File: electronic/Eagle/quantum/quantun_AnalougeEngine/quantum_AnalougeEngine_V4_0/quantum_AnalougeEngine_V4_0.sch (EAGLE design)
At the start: 167 parts, among them IC1 OP275, IC10 NE5532D, IC2 NE5532D, IC3 NE5532D, IC4 OP275, IC5 NE5532D, IC6 NE5532D, IC7 NE5532D, IC8 OP275, IC9 TL072, K5 RELAY_EE2-5NU, K6 RELAY_EE2-5NU, K7 RELAY_EE2-5NU, K8 RELAY_EE2-5NU, U1 NUCLEO-F429ZI, U12 ULN2003, U4 THAT1240, U6 THAT1240, U7 THAT1240, U8 THAT1240

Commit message: quantum_AnalougueEngine V4_0
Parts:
- removed C59, C64: 100nF, C_Sager_Bibliothek:CAPACITOR"
- removed C69, C70: 2.2µF, C_Sager_Bibliothek:SMD_ELCTROLYTIC
- removed D1, D2, D3, D4, D5, D6, D7, D8: 4148, C_Sager_Bibliothek:4148
- removed IC10, IC6: NE5532D, linear:NE5532D
- removed TP04: TPTHT, C_Sager_Bibliothek:TPTHT
- added C33, C34, C39, C40, C44: 10 µF, C_Sager_Bibliothek:ELECTROLYTHICELCTROLYTIC_MIDSIZE_SMD
- added C35, C36, C43, C45, C46, C47, C48, C49, C50: 100nF, C_Sager_Bibliothek:CAPACITOR"
- added C37, C38: 22pF, C_Sager_Bibliothek:CAPACITOR"
- added R36, R37: 20k, C_Sager_Bibliothek:RESISTOR
- added R38, R41, R44, R64: 51k, C_Sager_Bibliothek:RESISTOR
- added R39, R42, R45, R65: 51R, C_Sager_Bibliothek:RESISTOR
- added R40, R43, R63, R66: 90k9, C_Sager_Bibliothek:RESISTOR
- added R46, R68, R69, R70, R71, R72, R73, R74, R75: 10k, C_Sager_Bibliothek:RESISTOR
- added R47, R76: 1k8, C_Sager_Bibliothek:RESISTOR
- added R77: 0R, C_Sager_Bibliothek:RESISTOR
- added STAGE(LEFT), STAGE(RIGHT): THAT2181S, THAT_Library:THAT2181S
- added U$4: AD7606_EVALBOARD, C_Sager_Bibliothek:AD7606_EVALBOARD
- added Z1: BZT52C2V0T-7, C_Sager_Bibliothek:BZT52C2V0T-7
- C10, C16, C17, C9: value 100nF -> 470 pF
- C15, C18: value 100nF -> 47 pF
- C31, C32: value 100nF -> 10 µF; device C_Sager_Bibliothek:CAPACITOR" -> C_Sager_Bibliothek:ELECTROLYTHICELCTROLYTIC_MIDSIZE_SMD
- C67, C68: device C_Sager_Bibliothek:SMD_ELCTROLYTIC -> C_Sager_Bibliothek:ELECTROLYTHICELCTROLYTIC_MIDSIZE_SMD
- IC2, IC3: value NE5532D -> DAC084S085CIMM_NOPB; device linear:NE5532D -> SPI:DAC084S085CIMM_NOPB; SPICEPREFIX Z -> (none)
- IC5: value NE5532D -> OP275; device linear:NE5532D -> C_Sager_Bibliothek:OP275; SPICEPREFIX Z -> (none)
- IC7: value NE5532D -> TL072; device linear:NE5532D -> C_Sager_Bibliothek:TL072; SPICEPREFIX Z -> (none)
- K1: value RELAY_EE2-5NU -> K1
- K2: value RELAY_EE2-5NU -> K2
- K3: value RELAY_EE2-5NU -> K3
- K4: value RELAY_EE2-5NU -> K4
- R1, R16, R17, R23, R25, R27, R4, R6: value 100k -> 10k; device C_Sager_Bibliothek:RESISTOR" -> C_Sager_Bibliothek:RESISTOR
- R10, R11, R12, R2, R33, R34, R35, R48, R49, R50, R51, R52, R53, R9: device C_Sager_Bibliothek:RESISTOR" -> C_Sager_Bibliothek:RESISTOR
- R13, R18, R20, R22: value 100k -> 10k; device C_Sager_Bibliothek:RESISTOR" -> C_Sager_Bibliothek:RESISTOR; SPICEPREFIX (none) -> R
- R14, R29: value 0R -> 220R; device C_Sager_Bibliothek:RESISTOR" -> C_Sager_Bibliothek:RESISTOR
- R15, R24: value 0R -> 10k; device C_Sager_Bibliothek:RESISTOR" -> C_Sager_Bibliothek:RESISTOR
- R19: value 0R -> 10k; device C_Sager_Bibliothek:RESISTOR" -> C_Sager_Bibliothek:RESISTOR; SPICEPREFIX (none) -> R
- R21, R5: value 180k -> 10k; device C_Sager_Bibliothek:RESISTOR" -> C_Sager_Bibliothek:RESISTOR; SPICEPREFIX (none) -> R
- R26: value 180k -> 10k; device C_Sager_Bibliothek:RESISTOR" -> C_Sager_Bibliothek:RESISTOR
- R28: value 100k -> 20k; device C_Sager_Bibliothek:RESISTOR" -> C_Sager_Bibliothek:RESISTOR
- R3: value 0R -> 100k; device C_Sager_Bibliothek:RESISTOR" -> C_Sager_Bibliothek:RESISTOR; SPICEPREFIX (none) -> R
- R30: value 180k -> 20k; device C_Sager_Bibliothek:RESISTOR" -> C_Sager_Bibliothek:RESISTOR
- R31, R32: value 100k -> 5k1; device C_Sager_Bibliothek:RESISTOR" -> C_Sager_Bibliothek:RESISTOR
- R54, R58: value 2k00 -> 10k; device C_Sager_Bibliothek:RESISTOR" -> C_Sager_Bibliothek:RESISTOR
- R55, R61: value 178k -> 10k; device C_Sager_Bibliothek:RESISTOR" -> C_Sager_Bibliothek:RESISTOR
- R56: value 6k49 -> 10k; device C_Sager_Bibliothek:RESISTOR" -> C_Sager_Bibliothek:RESISTOR
- R57, R60: value 6k34 -> 10k; device C_Sager_Bibliothek:RESISTOR" -> C_Sager_Bibliothek:RESISTOR
- R59: value 6k49 -> 56k; device C_Sager_Bibliothek:RESISTOR" -> C_Sager_Bibliothek:RESISTOR
- R62, R67: value 51R -> 10k; device C_Sager_Bibliothek:RESISTOR" -> C_Sager_Bibliothek:RESISTOR
- R7, R8: device C_Sager_Bibliothek:RESISTOR" -> C_Sager_Bibliothek:RESISTOR; SPICEPREFIX (none) -> R
- U$1: value 7809 -> 7812
- renumbered BY_1_1 to K1, BY_1_2 to K2, BY_2_1 to K4, BY_2_2 to K3
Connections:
- net +9V renamed +12V
- removed net N$38: D5.C, D8.A, IC3A.OUT
- removed net N$39: D5.A, R25.1, R27.2
- removed net N$40: IC3B.-IN, R25.2, R26.2, R28.1
- removed net N$41: IC3B.OUT, R24.1, R28.2
- removed net N$42: D7.C, IC6A.-IN, R2.2, R31.1
- removed net N$44: D6.C, D7.A, IC6A.OUT
- removed net N$82: C59.2, IC9G$2.OUT, R54.2, TP36.TP, VCA2(RIGHT).EC+
- removed net N$84: C64.1, IC9G$1.-IN, R58.1, R59.2, R61.2
- removed net N$85: C69.+, R56.1, R57.2
- removed net N$87: R62.1, VCA1(LEFT).SYM
- removed net N$88: C64.2, IC9G$1.OUT, R58.2, TP37.TP, VCA1(LEFT).EC+
- removed net N$95: R67.1, VCA2(RIGHT).SYM
- removed net NET1: IC10A.-IN, IC10A.OUT, R17.1, R21.1
- removed net NET11: IC7A.-IN, IC7A.OUT, R1.1, R5.1
- removed net NET2: IC10B.-IN, IC10B.OUT, R18.1, R26.1
- removed net NET22: IC7B.-IN, IC7B.OUT, R2.1, R30.1
- removed net PF6: U1G$5.PF6
- new net +3V3_STM32: R1.2, U1G$5.+3.3V
- new net +5V_STM32: C19.1, C31.+, C43.1, C44.+, IC2.VA, IC3.VA, U$4.+5V, U1G$5.+5V
- new net .: IC7G$2.OUT, R59.2, R72.2
- new net ...: IC7G$1.OUT, R71.2, R73.2
- new net 0,5V_DAC: IC7G$1.+IN, IC7G$2.+IN, R60.2, R61.1
- new net 1V_DAC: C20.1, C23.1, C24.1, C32.+, C33.+, C34.+, IC2.VREFIN, IC3.VREFIN, R61.2, R68.1, R69.2
- new net 2V_DAC_REF: R67.1, R68.2, Z1.K
- new net BUSY: U$4.BUSY, U1G$5.PG3
- new net CHASIS: C15.1, C18.1, OUT1(R/S).G, OUT2(L/M).G, R77.1, TP03.TP
- new net CS: U$4.CS, U1G$5.PD7
- new net CS_DAC1: IC2.!SYNC, U1G$6.PB4
- new net CS_DAC2: IC3.!SYNC, U1G$6.PB5
- new net CV_A_B: U$4.CVA, U$4.CVB, U1G$5.PC12
- new net DAC2_OUT1(OFFSET_VCA1): C39.+, IC9G$1.+IN, R74.2, R76.2
- new net DAC2_OUT2(OFFSET_VCA2): C40.+, IC9G$2.+IN, R47.2, R75.2
- new net DAC2_OUT3: IC3.VOUTC, R62.1
- new net DAC2_OUT4: IC3.VOUTD, R70.1
- new net DB0: U$4.DB0, U1G$4.D34/PE0/TIMER_B_ETR, U1G$6.PE0
- new net DB1: U$4.DB1, U1G$5.PE1
- new net DB10: U$4.DB10, U1G$4.D40/PE10/TIMER_A_PWM2N, U1G$6.PE10
- new net DB11: U$4.DB11, U1G$4.D5/PE11/TIMER_A_PWM2
- new net DB12: U$4.DB12, U1G$4.D39/PE12/TIMER_A_PWM3N, U1G$6.PE12
- new net DB13: U$4.DB13, U1G$4.D3/PE13/TIMER_A_PWM3, U1G$6.PE13
- new net DB14: U$4.DB14, U1G$4.D38/PE14, U1G$6.PE14
- new net DB15: U$4.DB15, U1G$6.PE15
- new net DB2: U$4.DB2, U1G$3.D56/PE2/SAI_A_MCLK, U1G$4.D31/PE2
- new net DB3: U$4.DB3, U1G$3.D60/PE3/SAI_B_SD, U1G$5.PE3
- new net DB4: U$4.DB4, U1G$3.D57/PE4/SAI_A_FS
- new net DB5: U$4.DB5, U1G$3.D58/PE5/SAI_A_SCK
- new net DB6: U$4.DB6, U1G$3.D59/PE6/SAI_A_SD, U1G$5.PE6
- new net DB7: U$4.DB7, U1G$4.D41/PE7/TIMER_A_ETR, U1G$6.PE7
- new net DB8: U$4.DB8, U1G$4.D42/PE8/TIMER_A_PWM1N
- new net DB9: U$4.DB9, U1G$4.D6/PE9/TIMER_A_PWM1, U1G$6.PE9
- new net DIN_DAC: IC2.DIN, IC3.DIN, U1G$3.A2/PC3
- new net E+_OUT_STAGE_LEFT: R46.2, R73.1, STAGE(LEFT).EC+, TP02.TP
- new net E+_OUT_STAGE_RIGHT: R58.2, R59.1, STAGE(RIGHT).EC+, TP01.TP
- new net EC+_VCA1(LFT): IC9G$1.OUT, R56.2, TP37.TP, VCA1(LEFT).EC+
- new net EC+_VCA2(RIGHT): IC9G$2.OUT, R54.2, TP36.TP, VCA2(RIGHT).EC+
- new net FRST: U$4.FRST, U1G$5.PD6
- new net L/M_OUT(OUT_STAGE_LEFT): C37.2, IC1A.+IN, IC5A.OUT, K62.O, R19.1, R28.2
- new net N$53: C38.1, IC5B.-IN, R30.1, STAGE(RIGHT).OUT
- new net N$54: C45.1, R32.2, STAGE(RIGHT).V-
- new net N$55: R36.2, STAGE(LEFT).IN
- new net N$56: IC2.VOUTA, R38.2
- new net N$57: IC2.VOUTB, R41.2
- new net N$58: IC2.VOUTC, R44.2
- new net N$59: IC2.VOUTD, R64.2
- new net N$60: IC3.VOUTA, R74.1
- new net N$61: IC3.VOUTB, R75.1
- new net N$63: IC9G$1.-IN, R56.1, R57.2
- new net N$68: R37.2, STAGE(RIGHT).IN
- new net N$73: C48.1, R31.2, STAGE(LEFT).V-
- new net N$74: IC7G$2.-IN, R70.2, R72.1
- new net OS0: U$4.OS0, U1G$6.PC8
- new net OS1: U$4.OS1, U1G$6.PC9
- new net OS2: U$4.OS2, U1G$5.PC10
- new net R/S_OUT(OUT_STAGE_RIGHT): C38.2, IC1B.+IN, IC5B.OUT, K63.O, R20.1, R30.2
- new net RANGE: U$4.RANGE, U1G$5.PC11
- new net RD: U$4.RD, U1G$5.PD2
- new net RESET: U$4.RST, U1G$5.PG2
- new net SCLK_DAC: IC2.SCLK, IC3.SCLK, U1G$6.PB10
- new net SYM1: R38.1, R39.2, R40.2, VCA1(LEFT).SYM
- new net SYM2: R41.1, R42.2, R43.2, VCA2(RIGHT).SYM
- new net SYM3: R44.1, R45.2, R63.2, STAGE(LEFT).SYM
- new net SYM4: R64.1, R65.2, R66.2, STAGE(RIGHT).SYM
- new net VIO: U$4.VIO
- net ADC1-IN0: now also R3.1, R4.2; no longer R19.2, TP01.TP
- net ADC1-IN3: now also R1.1, R2.2; no longer R3.2, TP03.TP
- net ADC2-IN10: no longer R15.2, TP04.TP
- net ADC2-IN9: no longer R24.2, TP02.TP
- net AGND: now also C32.-, C33.-, C34.-, C35.2, C36.2, C39.-, C40.-, C45.2, C46.2, C47.2, C48.2, C49.2, C50.2, R15.1, R16.1, R23.1, R24.1, R25.1, R26.1, R27.1, R39.1, R4.1, R42.1, R45.1, R46.1, R47.1, R58.1, R6.1, R60.1, R65.1, R69.1, R76.1, STAGE(LEFT).EC-, STAGE(LEFT).GND, STAGE(RIGHT).EC-, STAGE(RIGHT).GND, U$4.G1, U$4.G2, U$4.G3, U$4.G4, U$4.G5, U$4.G6, U$4.G7, U$4.G8, Z1.A; no longer C10.2, C15.2, C16.2, C17.2, C18.2, C19.2, C31.2, C32.2, C69.-, C70.-, C9.2, IC2A.+IN, IC2B.+IN, IC3A.+IN, IC3B.+IN, IC6A.+IN, IC6B.+IN, IC9G$1.+IN, IC9G$2.+IN, R62.2, R67.2
- net DAC_OUT1: now also R57.1; no longer R60.1
- net DAC_OUT2: now also R55.1; no longer R57.1
- net DGND: now also C19.2, C31.-, C43.2, C44.-, IC2.GND, IC3.GND, R77.2, U$4.GND
- net L/M_IN(VCA1_IN): now also R5.1; no longer IC10A.+IN
- net L/M_OUT(VCA1_OUT): now also R17.1, R36.1; no longer IC1A.+IN, IC7A.+IN, K62.O
- net N$1: now also C9.1
- net N$10: now also R16.2, R17.2, U$4.V3; no longer D3.A, R20.1, R22.2
- net N$12: now also R18.2, R23.2, U$4.V4; no longer D1.A, R4.1, R6.2
- net N$13: now also C16.1
- net N$19: now also K72.O, K82.S; no longer K72.S, K82.O
- net N$2: now also C10.2
- net N$20: now also R19.2, R24.2, U$4.V5; no longer IC2B.-IN, R20.2, R21.2, R23.1
- net N$3: now also C10.1, C15.2, C9.2; no longer D4.C, IC2A.-IN, R17.2, R22.1
- net N$34: now also R20.2, R25.2, U$4.V6; no longer IC5B.-IN, R13.1, R4.2, R5.2
- net N$35: now also R21.2, R26.2, U$4.V7; no longer IC2B.OUT, R19.1, R23.2
- net N$36: now also R22.2, R27.2, U$4.V8; no longer IC5B.OUT, R13.2, R3.1
- net N$37: now also U1G$2.+3.3V; no longer D8.C, IC3A.-IN, R18.2, R27.1
- net N$4: now also R5.2, R6.2, U$4.V1; no longer D3.C, D4.A, IC2A.OUT
- net N$46: now also R21.1; no longer D6.A, R16.1, R31.2
- net N$47: now also R22.1; no longer IC6B.-IN, R16.2, R30.2, R32.1
- net N$48: now also C37.1, IC5A.-IN, R28.1, STAGE(LEFT).OUT; no longer IC6B.OUT, R15.1, R32.2
- net N$5: now also K72.S, K82.O; no longer K72.O, K82.S
- net N$6: now also R13.2, R15.2, U$4.V2; no longer D2.C, IC5A.-IN, R1.2, R6.1
- net N$7: now also C17.2
- net N$72: now also IC7G$1.-IN, R62.2, R71.1; no longer C70.+, R59.1, R60.2
- net N$81: no longer C59.1, R56.2
- net N$9: now also C16.2, C17.1, C18.2; no longer D1.C, D2.A, IC5A.OUT
- net OUT_L/M: now also K82.P; no longer K72.P
- net OUT_R/S: now also K72.P; no longer K82.P
- net R/S_IN(VCA2_IN): now also R13.1; no longer IC10B.+IN
- net R/S_OUT(VCA2_OUT): now also R18.1, R37.1; no longer IC1B.+IN, IC7B.+IN, K63.O
- net RELAIS2: now also U1G$5.PG0; no longer U1G$5.PE6
- net V+: now also C35.1, C46.1, C47.1, C49.1, IC7G$3.V+, R3.2, R67.2, STAGE(LEFT).V+, STAGE(RIGHT).V+; no longer C10.1, C16.1, C18.1, C20.1, C23.1, C32.1, IC10P.V+, IC2P.V+, IC3P.V+, IC6P.V+, IC7P.V+
- net V-: now also C36.1, C50.1, IC7G$3.V-, R2.1, R31.1, R32.1, R40.1, R43.1, R63.1, R66.1; no longer C15.1, C17.1, C19.1, C24.1, C31.1, C9.1, IC10P.V-, IC2P.V-, IC3P.V-, IC6P.V-, IC7P.V-, R55.1, R61.1
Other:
- note added: "AD Converter"
- note added: "Attention SPI is not configured jet in CubeMX"
- note added: "DA Converter"
- note added: "OUT_Stage"
- note added: "OUT_Stage (left)"
- note added: "OUT_Stage (right)"
- note added: "could offset the main VCA by 153 mV which means about + 25,5 dB! step size is approx. 0.1dB per bit"
- note added: "creates CV: 0 75,75 mV +12,625 dB 128 0 mV 0 dB 255 -77,75 mV -12,625 dB"
- note added: "from input section"
- note added: "measure negative supply voltage"
- note added: "measure positive supply voltage"
- note added: "use: SPI2: Transmit Only Master PB10: SPI2_SCK PC3: SPI2_MOSI PB4: CS_DAC1 PB5: CS_DAC2"
- note removed: "Präzisionsgleichrichter"

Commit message: minor updates on quantum_AnlougeEngine_V4_0
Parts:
- removed +15VOK, -15VOK, L1, L2, L3, L4, L5, L6, L7, L8: SMD_LED_0603, C_Sager_Bibliothek:SMD_LED_0603
- added LED1, LED2, LED3, LED4, LED5, LED6, LED7, LED8: LED_BLUE_SMD, C_Sager_Bibliothek:LED_BLUE_SMD
- added LED10, LED9: LED_GREEN_SMD, C_Sager_Bibliothek:LED_GREEN_SMD
- added TP04: TPTHT, C_Sager_Bibliothek:TPTHT
- C31, C32, C33, C34, C39, C40, C44, C67, C68: device C_Sager_Bibliothek:ELECTROLYTHICELCTROLYTIC_MIDSIZE_SMD -> C_Sager_Bibliothek:ELECTROLYTICELCTROLYTIC_MIDSIZE_SMD
- C69: value (none) -> 0.33 uF
- C70: value (none) -> 100 nF
- IN_LEFT, IN_RIGHT, U4, U6, U7, U8: device THAT_Library:THAT1240SO8-U -> THAT_Library:THAT1240SO8-USO8-U
- K5: value RELAY_EE2-5NU -> K5
- K6: value RELAY_EE2-5NU -> K6
- K7: value RELAY_EE2-5NU -> K7
- K8: value RELAY_EE2-5NU -> K8
- OUT_LEFT, OUT_RIGHT: device THAT_Library:THAT1646SO8-U -> THAT_Library:THAT1646SO8-USO8-U
- R10, R11, R12, R33, R34, R7, R8, R9: value 500R -> 470R
- STAGE(LEFT), STAGE(RIGHT), VCA1(LEFT), VCA2(RIGHT): value THAT2181S -> THAT2181SO8-US; device THAT_Library:THAT2181S -> THAT_Library:THAT2181SO8-US
- renumbered U$1 to U2, U$2 to C69, U$3 to C70, U$4 to U3
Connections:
- new net BOTTOM: TP06.TP
- net +12V: now also LED1.+, LED2.+, LED3.+, LED4.+, LED5.+, LED6.+, LED7.+, LED8.+; no longer L1.+, L2.+, L3.+, L4.+, L5.+, L6.+, L7.+, L8.+
- net AGND: now also LED9.-, TP04.TP; no longer +15VOK.-, TP06.TP
- net N$14: now also LED1.-; no longer L1.-
- net N$16: now also LED3.-; no longer L3.-
- net N$26: now also LED8.-; no longer L8.-
- net N$29: now also LED7.-; no longer L7.-
- net N$30: now also LED6.-; no longer L6.-
- net N$32: now also LED5.-; no longer L5.-
- net N$49: now also LED2.-; no longer L2.-
- net N$50: now also LED10.+; no longer -15VOK.+
- net N$51: now also LED4.-; no longer L4.-
- net N$52: now also LED9.+; no longer +15VOK.+
- net V-: now also LED10.-; no longer -15VOK.-
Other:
- moved on the sheet: TP06

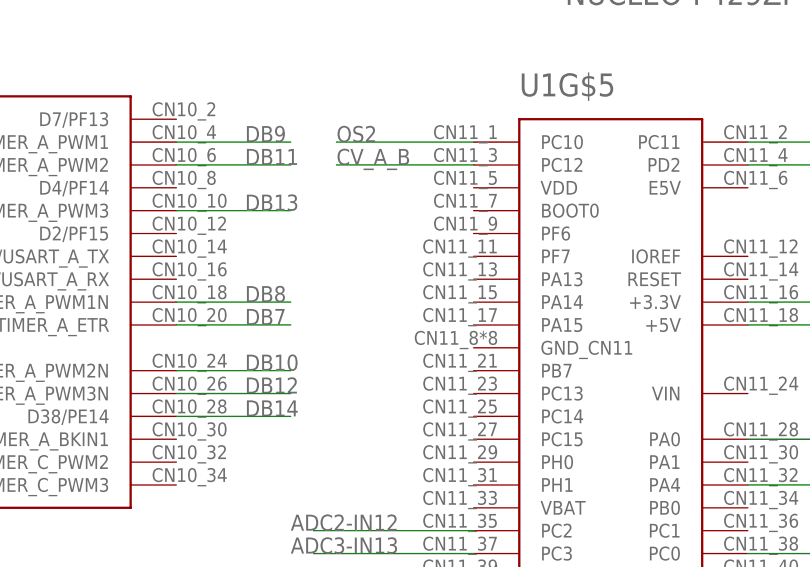
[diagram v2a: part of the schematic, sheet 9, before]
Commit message: Clock changed to 8 MHz Crystal. Progress AnalougeEngine (routing 50 %).
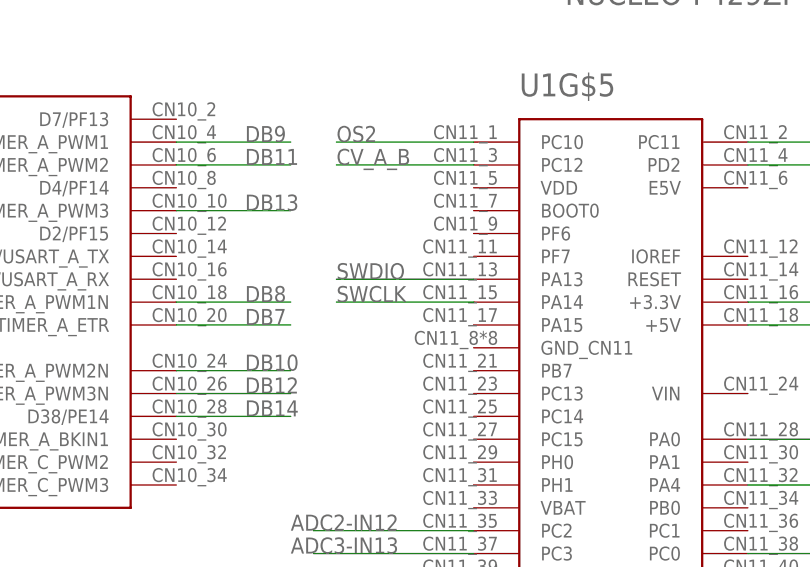
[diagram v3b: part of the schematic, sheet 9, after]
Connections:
- new net SWCLK: U1G$5.PA14
- new net SWDIO: U1G$5.PA13
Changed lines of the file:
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@@
+</segment>
+</net>
+<net name="SWCLK" class="0">
+<segment>
+<pinref part="U1" gate="G$5" pin="PA14"/>
+<wire x1="129.54" y1="104.14" x2="114.3" y2="104.14" width="0.1524" layer="91"/>
+<label x="114.3" y="104.14" size="1.778" layer="95"/>
+</segment>
+</net>
+<net name="SWDIO" class="0">
+<segment>
+<pinref part="U1" gate="G$5" pin="PA13"/>
+<wire x1="129.54" y1="106.68" x2="114.3" y2="106.68" width="0.1524" layer="91"/>
+<label x="114.3" y="106.68" size="1.778" layer="95"/>
 </segment>
 </net>
